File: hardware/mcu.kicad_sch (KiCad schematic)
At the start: 22 parts, among them SW1 SW_Push, SW4 SW_Push, U1 STM32L072RBTx

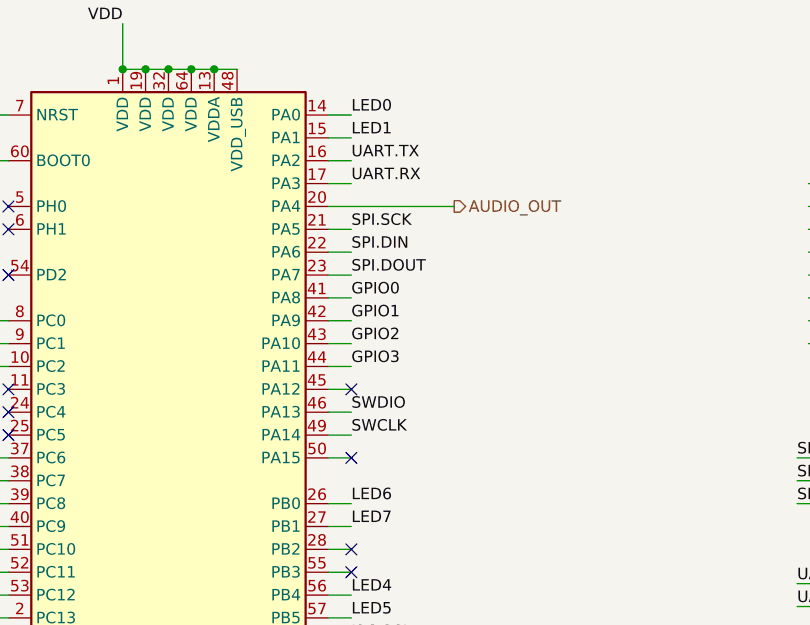
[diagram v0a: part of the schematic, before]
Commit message: [Hardware] Update MCU pinout.
* Move UART RX to PA15
* Route audio input to PA3 in addition to PC0
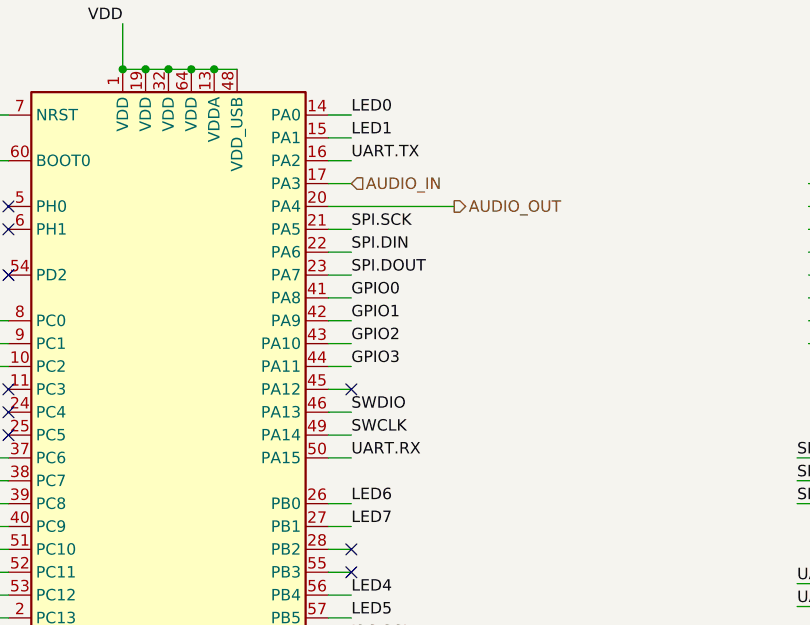
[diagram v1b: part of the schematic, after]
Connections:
- net AUDIO_IN: now also U1.17 (PA3)
- net UART.RX: now also U1.50 (PA15); no longer U1.17 (PA3)
- no-connect marks 13 -> 12
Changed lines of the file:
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@@
-	)
-	(no_connect
-		(at 160.02 83.82)
 	)
 	(no_connect
@@
 	(wire
 		(pts
+			(xy 157.48 83.82) (xy 160.02 83.82)
+		)
+		(stroke
+			(width 0)
+			(type default)
+		)
+	)
+	(wire
+		(pts
 			(xy 157.48 116.84) (xy 160.02 116.84)
 		)
@@
 	(wire
 		(pts
+			(xy 157.48 53.34) (xy 160.02 53.34)
+		)
+		(stroke
+			(width 0)
+			(type default)
+		)
+	)
+	(wire
+		(pts
 			(xy 217.17 30.48) (xy 219.71 30.48)
 		)
@@
 	(wire
 		(pts
-			(xy 157.48 53.34) (xy 160.02 53.34)
-		)
-		(stroke
-			(width 0)
-			(type default)
-		)
-	)
-	(wire
-		(pts
 			(xy 157.48 124.46) (xy 160.02 124.46)
 		)
@@
 		(pts
 			(xy 157.48 55.88) (xy 171.45 55.88)
-		)
-		(stroke
-			(width 0)
-			(type default)
-		)
-	)
-	(wire
-		(pts
-			(xy 157.48 83.82) (xy 160.02 83.82)
 		)
 		(stroke
@@
 	)
 	(label "UART.RX"
-		(at 160.02 53.34 0)
+		(at 160.02 83.82 0)
 		(fields_autoplaced yes)
 		(effects
@@
 		)
 	)
+	(hierarchical_label "AUDIO_IN"
+		(shape input)
+		(at 160.02 53.34 0)
+		(fields_autoplaced yes)
+		(effects
+			(font
+				(size 1.27 1.27)
+			)
+			(justify left)
+		)
+	)

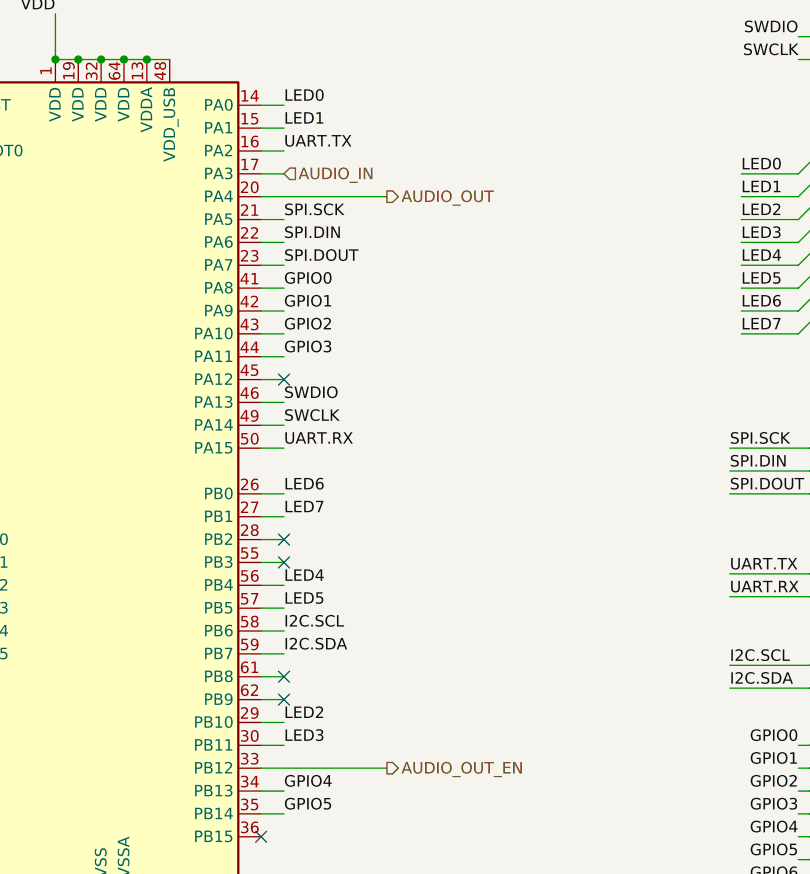
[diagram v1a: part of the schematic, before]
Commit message: [Hardware] Add amplifier to microphone output.
The STM32 part we are using does not include an internal opamp, so we are adding an external opamp to bias and amplify the audio signal.

* Add opamp opa355
* calculate resistor network for gain of 10
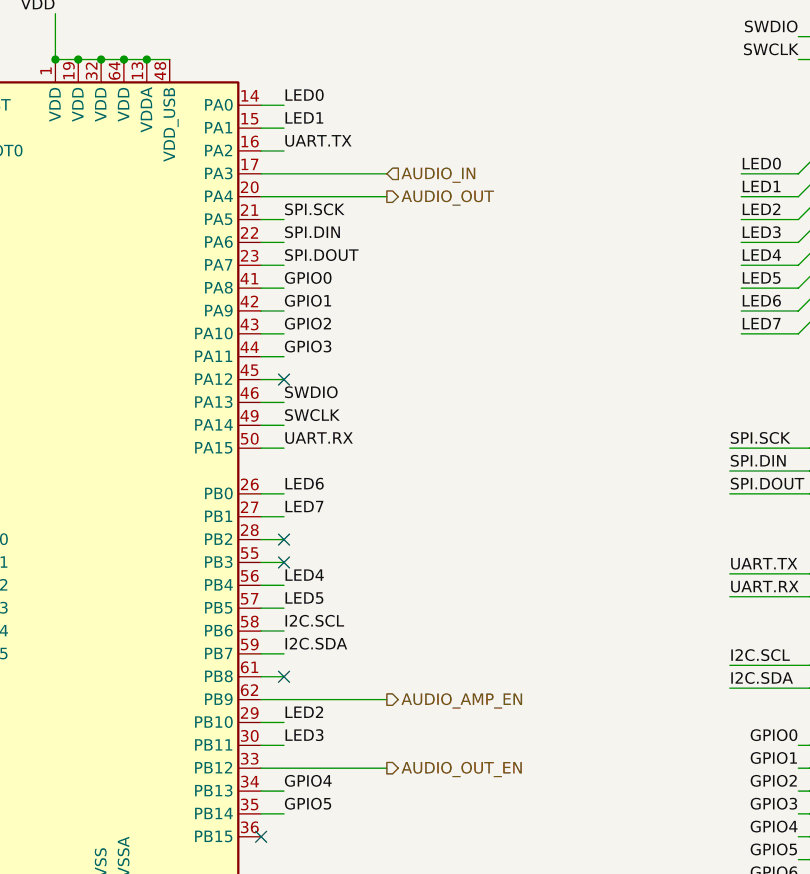
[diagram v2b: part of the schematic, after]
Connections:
- net AUDIO_AMP_EN: now reaches U1.62 (PB9)
- no-connect marks 12 -> 11
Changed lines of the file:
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@@
-	)
-	(no_connect
-		(at 160.02 111.76)
 	)
 	(no_connect
@@
 	(wire
 		(pts
+			(xy 157.48 111.76) (xy 171.45 111.76)
+		)
+		(stroke
+			(width 0)
+			(type default)
+		)
+	)
+	(wire
+		(pts
 			(xy 114.3 165.1) (xy 114.3 161.29)
 		)
@@
 	(wire
 		(pts
-			(xy 157.48 53.34) (xy 160.02 53.34)
+			(xy 157.48 53.34) (xy 171.45 53.34)
 		)
 		(stroke
@@
 		(pts
 			(xy 40.64 177.8) (xy 40.64 173.99)
-		)
-		(stroke
-			(width 0)
-			(type default)
-		)
-	)
-	(wire
-		(pts
-			(xy 157.48 111.76) (xy 160.02 111.76)
 		)
 		(stroke
@@
 		)
 	)
+	(hierarchical_label "AUDIO_AMP_EN"
+		(shape output)
+		(at 171.45 111.76 0)
+		(fields_autoplaced yes)
+		(effects
+			(font
+				(size 1.27 1.27)
+			)
+			(justify left)
+		)
+	)
 	(hierarchical_label "AUDIO_IN"
 		(shape input)
-		(at 160.02 53.34 0)
-		(fields_autoplaced yes)
-		(effects
+		(at 171.45 53.34 0)
+		(fields_autoplaced yes)
+		(effects

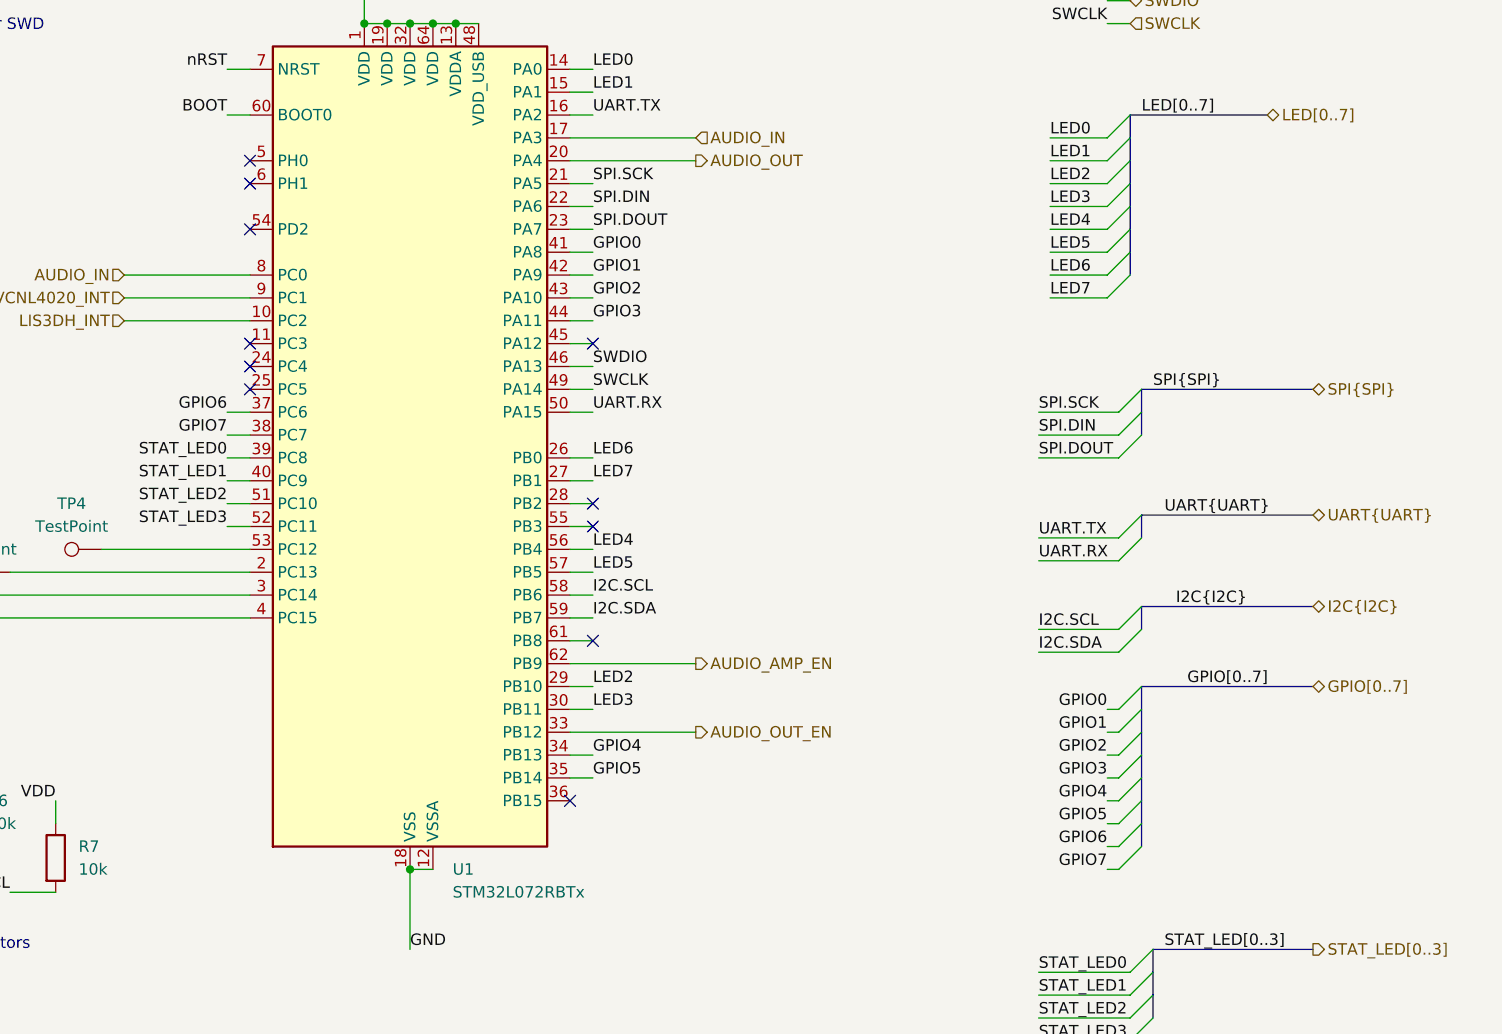
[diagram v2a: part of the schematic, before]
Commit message: [Hardware] Remove unused breakouts
* Remove extra GPIO and SPI outputs from MCU
* remove auxillary connectors for GPIO, SPI, and I2C
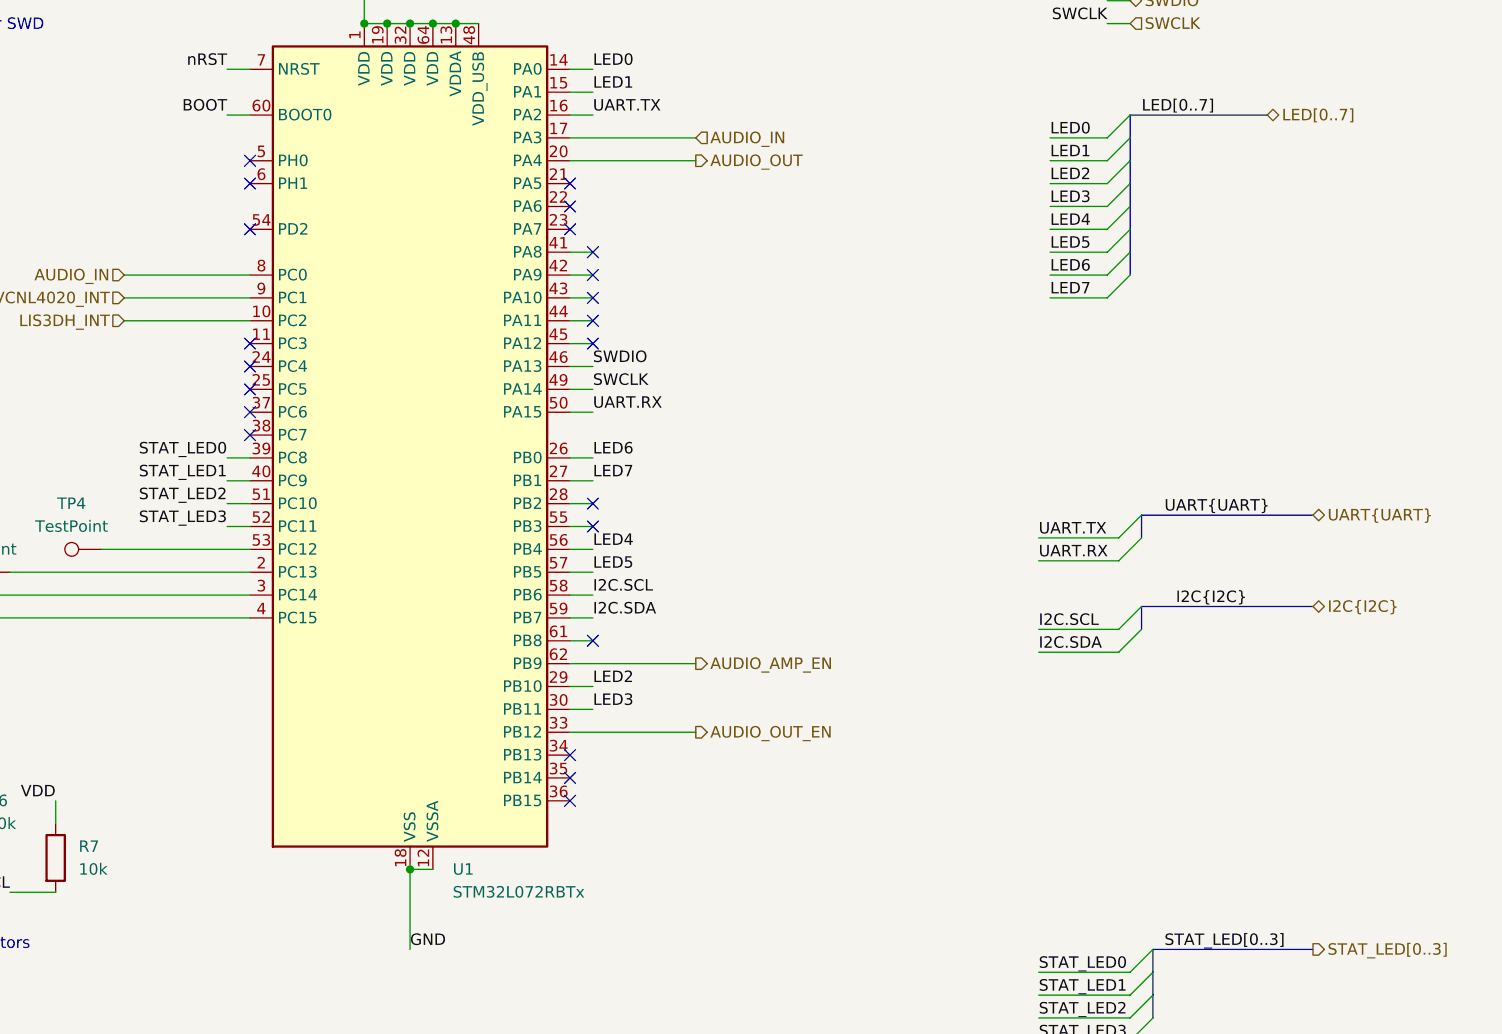
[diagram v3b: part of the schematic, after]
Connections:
- net GPIO0: no longer names the net of U1.41 (PA8)
- net GPIO1: no longer names the net of U1.42 (PA9)
- net GPIO2: no longer names the net of U1.43 (PA10)
- net GPIO3: no longer names the net of U1.44 (PA11)
- net GPIO4: no longer names the net of U1.34 (PB13)
- net GPIO5: no longer names the net of U1.35 (PB14)
- net GPIO6: no longer names the net of U1.37 (PC6)
- net GPIO7: no longer names the net of U1.38 (PC7)
- net SPI.DIN: no longer names the net of U1.22 (PA6)
- net SPI.DOUT: no longer names the net of U1.23 (PA7)
- net SPI.SCK: no longer names the net of U1.21 (PA5)
- no-connect marks 11 -> 22

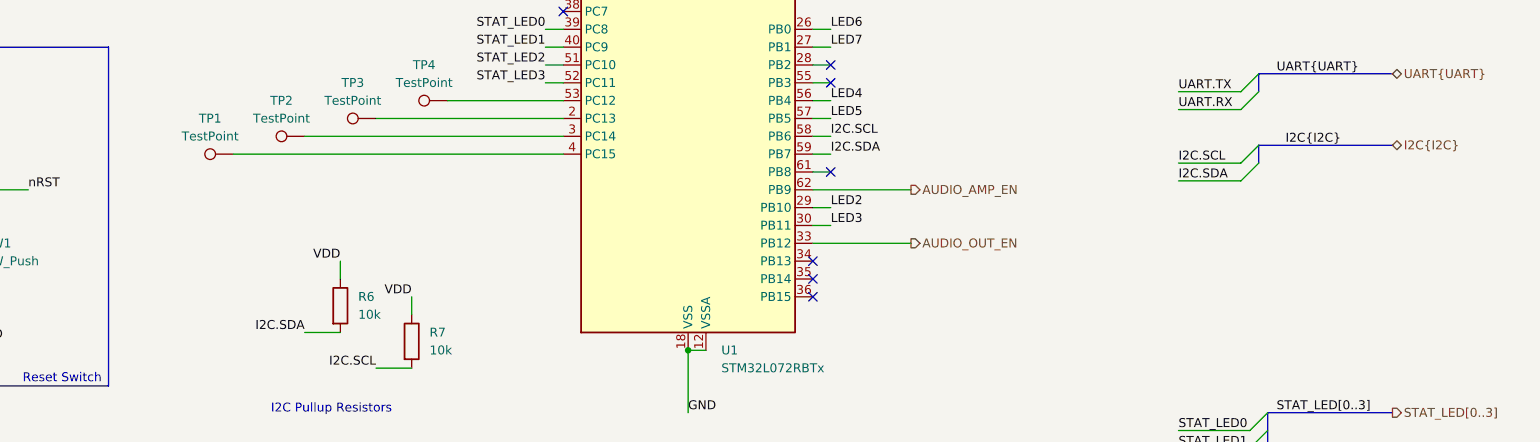
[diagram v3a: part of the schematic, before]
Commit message: [Hardware] Update testpoints
* Add TPs for I2C since we removed the I2C header
* Add ground testpoints for GPIO and audio out
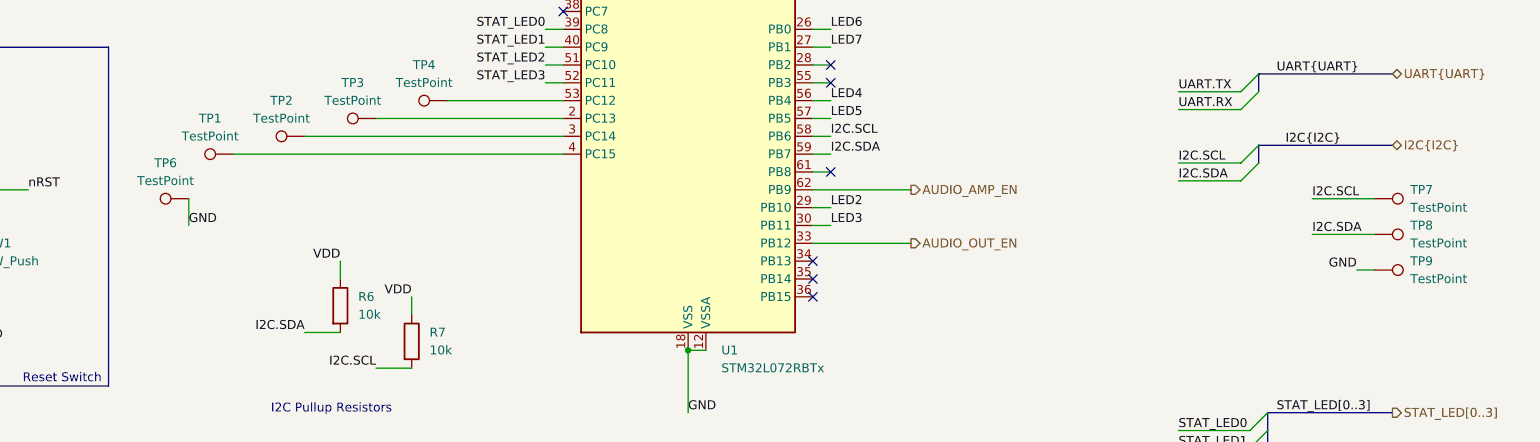
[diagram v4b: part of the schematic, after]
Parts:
- added TP6, TP7, TP8, TP9: TestPoint, Leaf_Jumper:TestPoint_0.5mm_1mm, symbol Connector:TestPoint
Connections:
- net GND: now also TP6.1, TP9.1
- net I2C.SCL: now also TP7.1
- net I2C.SDA: now also TP8.1
